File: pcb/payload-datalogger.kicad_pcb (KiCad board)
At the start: 2 copper layers, 50.5 x 41.5 mm, 42 parts, among them J1 2.54mm 01x02 header, J2 DE15 Socket, SW2 PTS815, U1 XIAO-ESP32-C3-DIP, U2 NCP177AMX330TCG, U3 W25X40CLSN, U4 MCP96RL00T-E_MX, U5 MCP96RL00T-E_MX, U6 MCP96RL00T-E_MX, U7 MCP96RL00T-E_MX

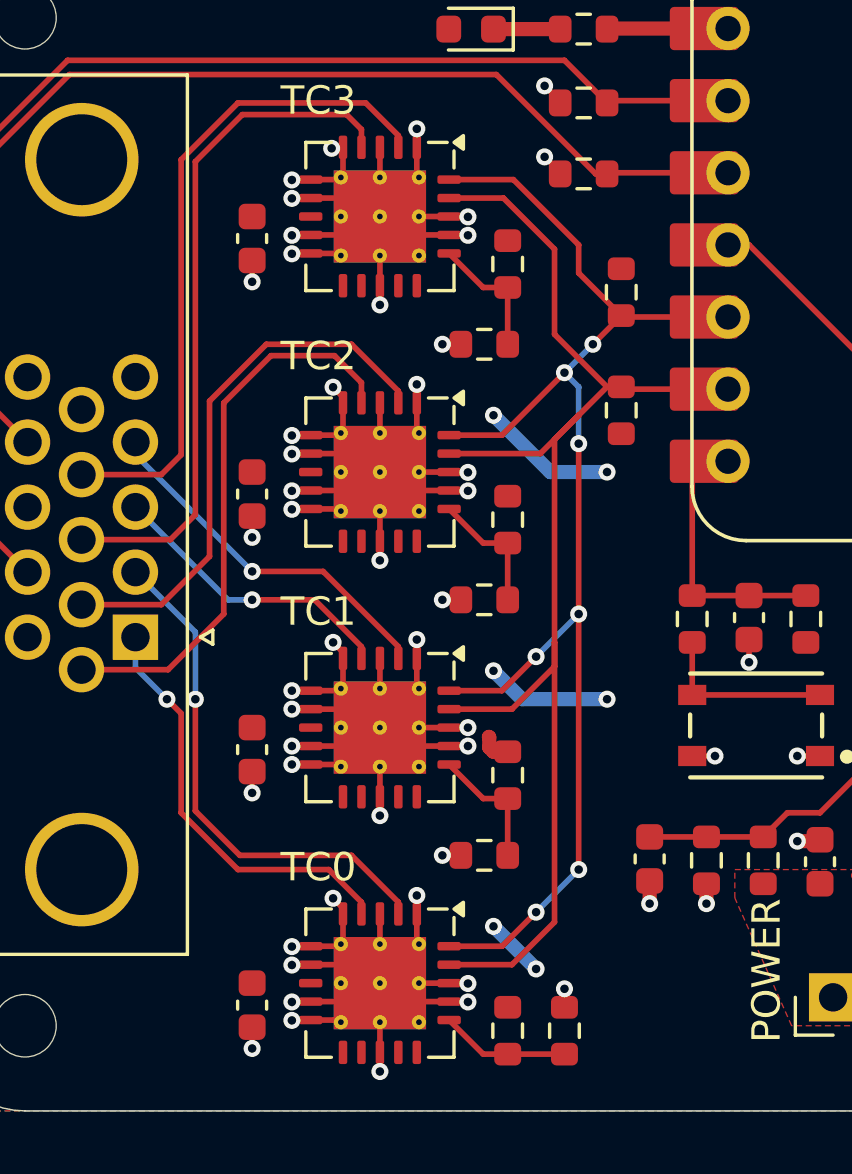
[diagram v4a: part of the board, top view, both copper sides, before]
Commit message: Increase thermal vias to 0.3mm hole
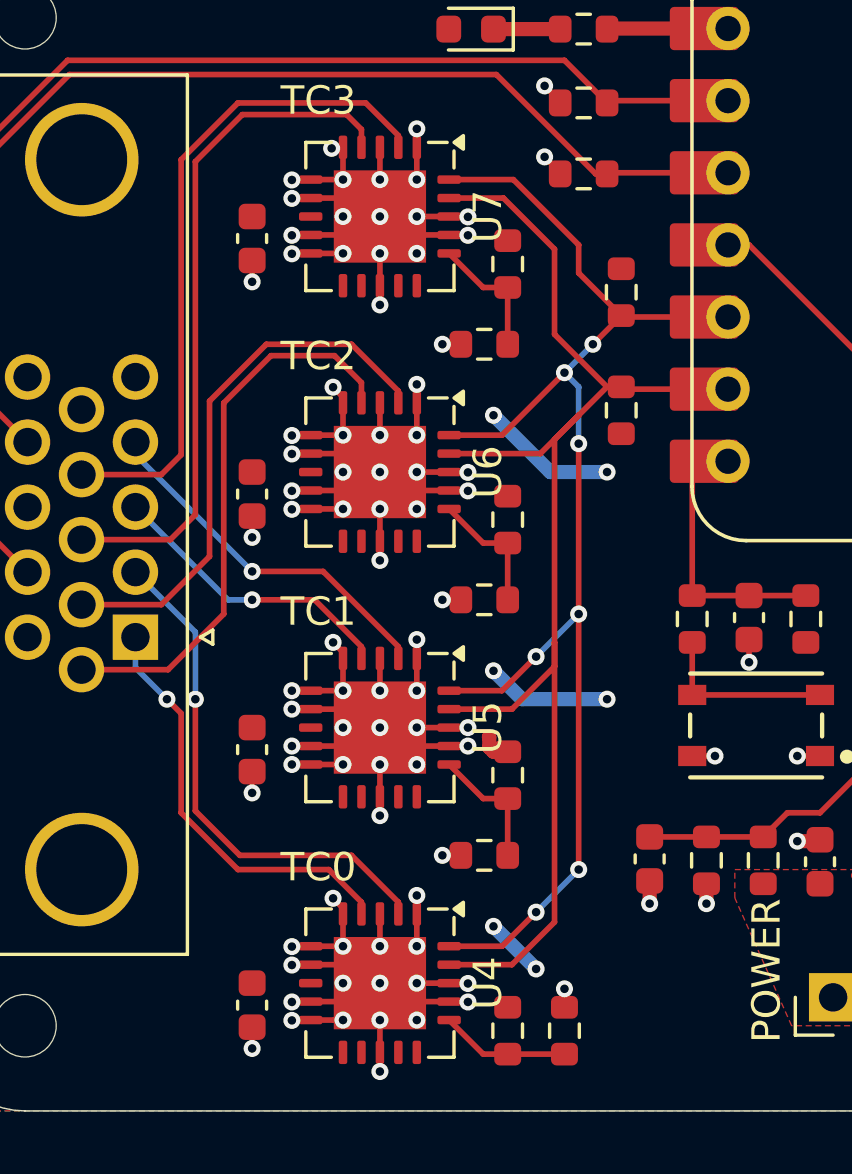
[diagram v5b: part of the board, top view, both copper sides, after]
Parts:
- U4, U5, U6, U7: footprint Package_DFN_QFN:TQFN-20-1EP_5x5mm_P0.65mm_EP3.25x3.25mm_ThermalVias -> Package_DFN_QFN:TQFN-20-1EP_5x5mm_P0.65mm_EP3.25x3.25mm
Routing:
- net GND: track 134.1 -> 124.5 mm, vias 56 -> 92

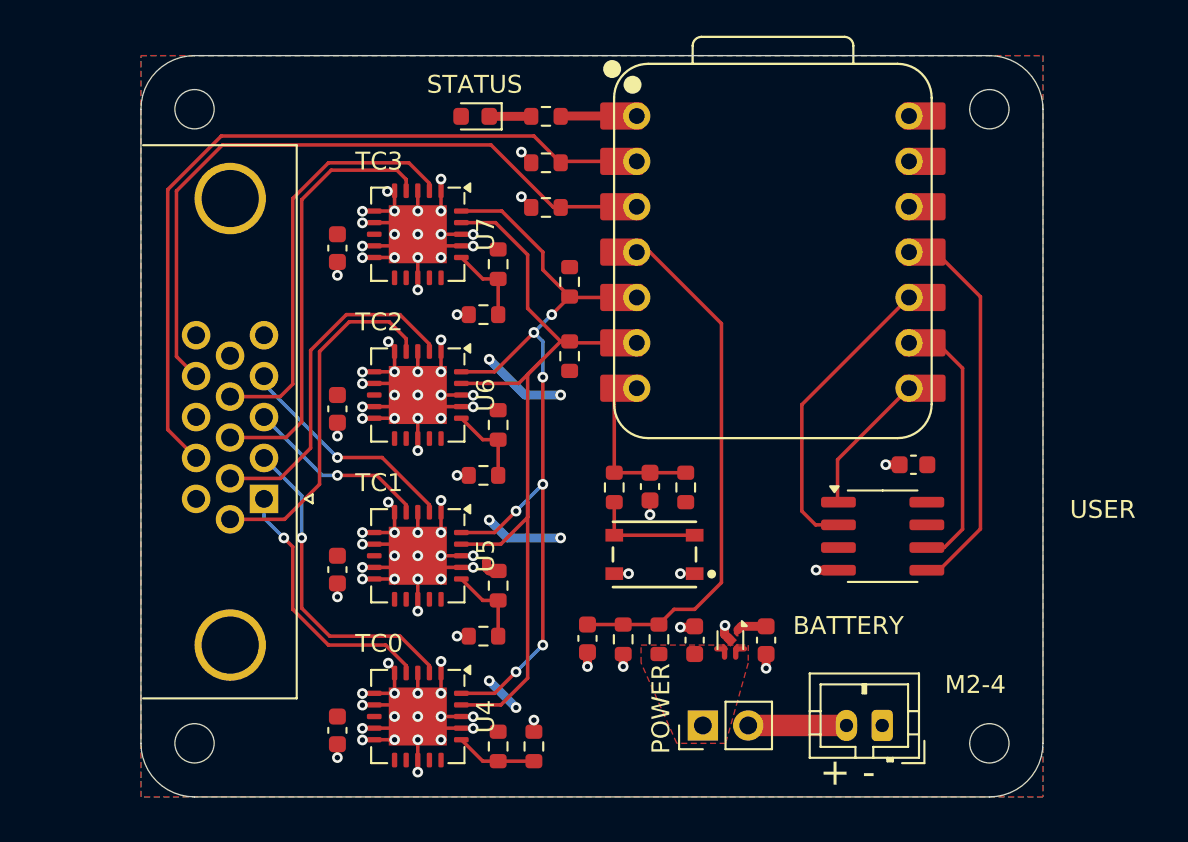
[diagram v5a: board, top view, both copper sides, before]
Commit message: Use larger Dsub for BOM optimization
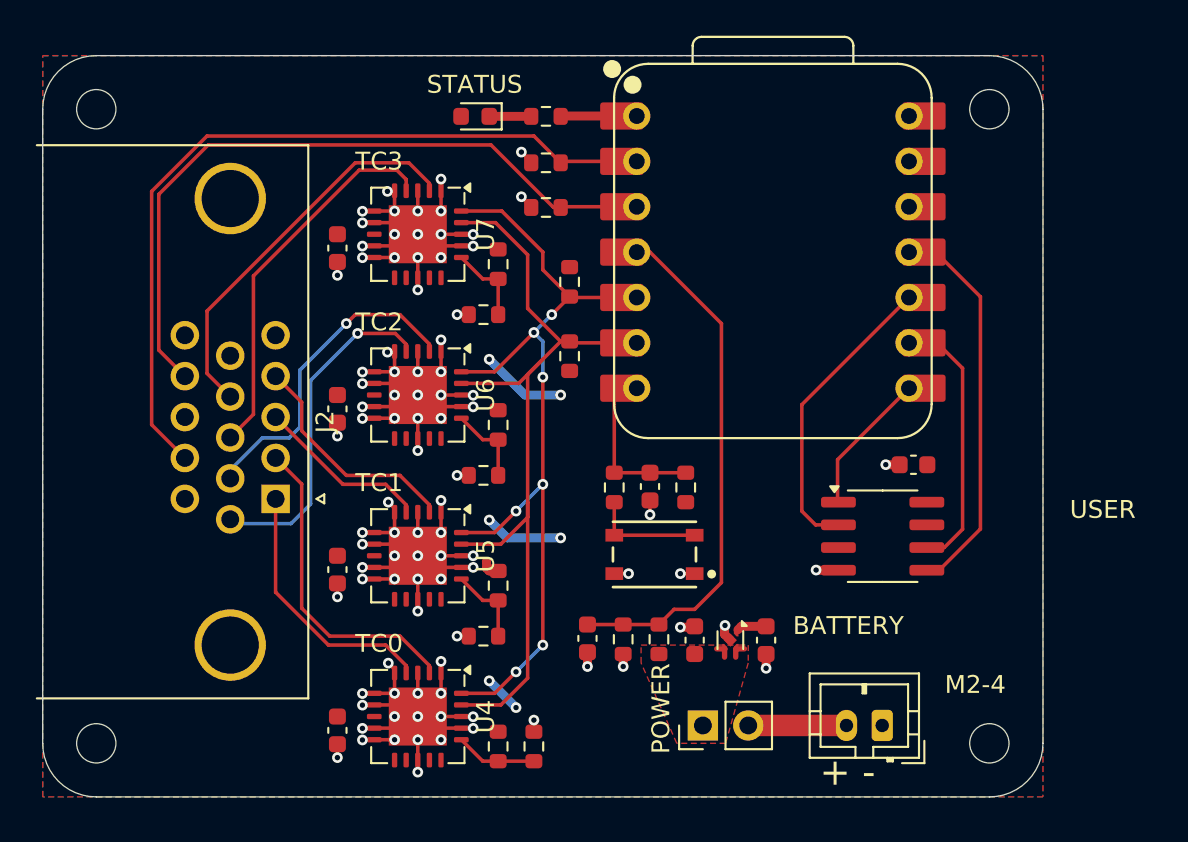
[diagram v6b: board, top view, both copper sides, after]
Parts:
- J2: footprint Connector_Dsub:DSUB-15-HD_Socket_Horizontal_P2.29x1.90mm_EdgePinOffset3.03mm_Housed_MountingHolesOffset4.94mm -> Connector_Dsub:DSUB-15-HD_Socket_Horizontal_P2.29x2.54mm_EdgePinOffset8.35mm_Housed_MountingHolesOffset10.89mm
- moved REF** 5.50 mm to (62.0, 77.5)
- moved REF** 5.50 mm to (62.0, 42.0)
- moved J2 0.65 mm to (72.0, 63.8)
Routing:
- net /TC3-: track 24.2 -> 21.4 mm
- net /TC3+: track 23.6 -> 22.1 mm
- net /TC2+: track 19.3 -> 18.2 mm, vias 0 -> 1
- net /NTC1-: track 38.3 -> 39.3 mm
- net /NTC0-: track 43.0 -> 44.0 mm
- net /TC2-: track 19.9 -> 19.1 mm, vias 0 -> 1
- net /TC1-: track 10.4 -> 9.76 mm, vias 1 -> 0
- net /TC0+: track 18.2 -> 17.9 mm, vias 1 -> 0
- net /TC0-: track 14.9 -> 14.6 mm, vias 1 -> 0
- net /TC1+: vias 1 -> 0
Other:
- board size 50.5 x 41.5 mm -> 56 x 41.5 mm

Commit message: Prevent mounting hole overlap with dsub
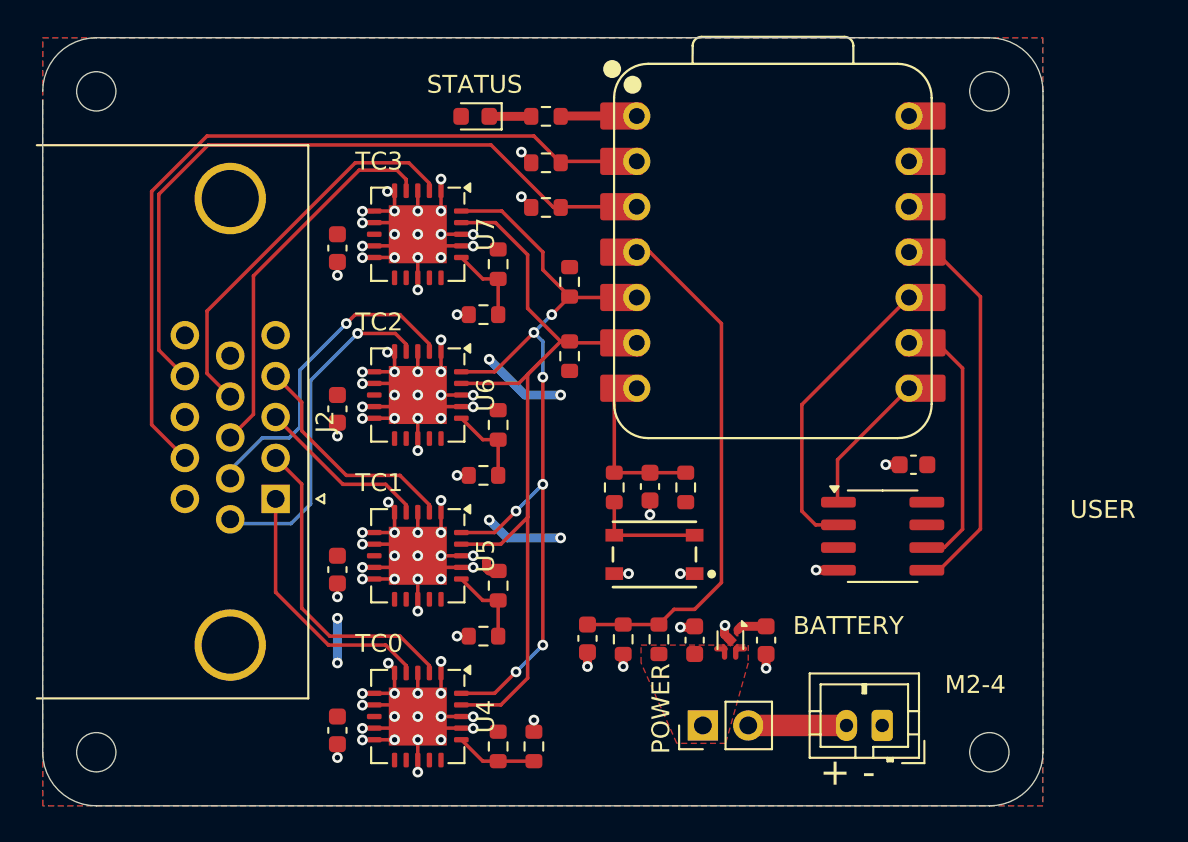
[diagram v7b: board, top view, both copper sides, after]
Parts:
- moved REF** 1.00 mm to (62.0, 41.0)
- moved REF** 1.00 mm to (112.0, 41.0)
- moved REF** 0.50 mm to (62.0, 78.0)
- moved REF** 0.50 mm to (112.0, 78.0)
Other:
- board size 56 x 41.5 mm -> 56 x 43 mm
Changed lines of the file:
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@@
 	(footprint "MountingHole:MountingHole_2.2mm_M2"
 		(layer "F.Cu")
-		(at 62 77.5)
+		(at 62 78)
 		(descr "Mounting Hole 2.2mm, no annular, M2")
 		(tags "mounting hole 2.2mm no annular m2")
@@
 	(footprint "MountingHole:MountingHole_2.2mm_M2"
 		(layer "F.Cu")
-		(at 62 42)
+		(at 62 41)
 		(descr "Mounting Hole 2.2mm, no annular, M2")
 		(tags "mounting hole 2.2mm no annular m2")
@@
 	(footprint "MountingHole:MountingHole_2.2mm_M2"
 		(layer "F.Cu")
-		(at 112 42)
+		(at 112 41)
 		(descr "Mounting Hole 2.2mm, no annular, M2")
 		(tags "mounting hole 2.2mm no annular m2")
@@
 	(footprint "MountingHole:MountingHole_2.2mm_M2"
 		(layer "F.Cu")
-		(at 112 77.5)
+		(at 112 78)
 		(descr "Mounting Hole 2.2mm, no annular, M2")
 		(tags "mounting hole 2.2mm no annular m2")
@@
 	)
 	(gr_line
-		(start 115 42)
-		(end 115 77.5)
+		(start 115 41)
+		(end 115 78)
 		(stroke
 			(width 0.05)
@@
 	)
 	(gr_line
-		(start 62 39)
-		(end 112 39)
+		(start 62 38)
+		(end 112 38)
 		(stroke
 			(width 0.05)
@@
 	)
 	(gr_arc
-		(start 59 42)
-		(mid 59.87868 39.87868)
-		(end 62 39)
+		(start 59 41)
+		(mid 59.87868 38.87868)
+		(end 62 38)
 		(stroke
 			(width 0.05)
@@
 	)
 	(gr_arc
-		(start 62 80.5)
-		(mid 59.87868 79.62132)
-		(end 59 77.5)
+		(start 62 81)
+		(mid 59.87868 80.12132)
+		(end 59 78)
 		(stroke
 			(width 0.05)
@@
 	)
 	(gr_arc
-		(start 115 77.5)
-		(mid 114.12132 79.62132)
-		(end 112 80.5)
+		(start 115 78)
+		(mid 114.12132 80.12132)
+		(end 112 81)
 		(stroke
 			(width 0.05)
@@
 	)
 	(gr_arc
-		(start 112 39)
-		(mid 114.12132 39.87868)
-		(end 115 42)
+		(start 112 38)
+		(mid 114.12132 38.87868)
+		(end 115 41)
 		(stroke
 			(width 0.05)
@@
 	)
 	(gr_line
-		(start 112 80.5)
-		(end 62 80.5)
+		(start 112 81)
+		(end 62 81)
 		(stroke
 			(width 0.05)
@@
 	)
 	(gr_line
-		(start 59 77.5)
-		(end 59 42)
+		(start 59 78)
+		(end 59 41.5)
 		(stroke
 			(width 0.05)
@@
 	)
 	(via
-		(at 85.5 75.5)
+		(at 75.5 73)
 		(size 0.6)
 		(drill 0.3)
@@
 	)
 	(via
-		(at 84 74)
+		(at 75.5 70.5)
 		(size 0.6)
 		(drill 0.3)
@@
 	)
 	(segment
+		(start 75.5 73)
+		(end 75.5 70.5)
+		(width 0.5)
+		(layer "B.Cu")
+		(net 3)
+	)
+	(segment
 		(start 88 66)
 		(end 85 66)
@@
 	)
 	(segment
-		(start 85.5 75.5)
-		(end 84 74)
-		(width 0.5)
-		(layer "B.Cu")
-		(net 3)
-	)
-	(segment
 		(start 86 58)
 		(end 84 56)
@@
 		(polygon
 			(pts
-				(xy 59 39) (xy 115 39) (xy 115 80.5) (xy 59 80.5)
+				(xy 59 38) (xy 115 38) (xy 115 81) (xy 59 81)
 			)
 		)
@@
 		(polygon
 			(pts
-				(xy 59 39) (xy 115 39) (xy 115 80.5) (xy 59 80.5)
+				(xy 59 38) (xy 115 38) (xy 115 81) (xy 59 81)
 			)
 		)
